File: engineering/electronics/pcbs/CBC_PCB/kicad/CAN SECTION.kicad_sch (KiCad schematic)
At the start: 44 parts, among them U25 ADM3053BRWZ-REEL7, U26 ADM3053BRWZ-REEL7, X1 8MHz, X2 8MHz

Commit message: fix: restore CBC schematic library nicknames
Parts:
- C10, C11, C3, C6: symbol CBC_PCB:CC0402JRNPO9BN220 -> EasyEDA_Lib:CC0402JRNPO9BN220
- C12, C48, C49, C5, C53, C54: symbol CBC_PCB:CL21A475KBQNNNE -> EasyEDA_Lib:CL21A475KBQNNNE
- C13, C4, C47, C50, C51, C55, C56, C57: symbol CBC_PCB:GRM21BR61H106KE43L -> EasyEDA_Lib:GRM21BR61H106KE43L
- C14, C2, C52, C58: symbol CBC_PCB:CC0402KRX7R7BB104 -> EasyEDA_Lib:CC0402KRX7R7BB104
- C16, C17, C8, C9: symbol CBC_PCB:GRM1555C1H221JA01D -> EasyEDA_Lib:GRM1555C1H221JA01D
- D1, D2: symbol CBC_PCB:NUP2105LT1G -> EasyEDA_Lib:NUP2105LT1G
- H1, H2: symbol CBC_PCB:PZ254V-11-02P -> EasyEDA_Lib:PZ254V-11-02P
- L1, L2: symbol CBC_PCB:ACT45B-510-2P-TF -> EasyEDA_Lib:ACT45B-510-2P-TF
- R1, R4: symbol CBC_PCB:0603WAF1200T5E -> EasyEDA_Lib:0603WAF1200T5E
- R2, R3: symbol CBC_PCB:RT0402BRD0710KL -> EasyEDA_Lib:RT0402BRD0710KL
- R34, R35: symbol CBC_PCB:RC0402FR-070RL -> EasyEDA_Lib:RC0402FR-070RL
- U25, U26: symbol CBC_PCB:ADM3053BRWZ-REEL7 -> EasyEDA_Lib:ADM3053BRWZ-REEL7
- U3, U5: symbol CBC_PCB:MCP2515T-I/ST -> EasyEDA_Lib:MCP2515T-I/ST
- X1, X2: symbol CBC_PCB:H1OEL89CSC-SUGYLC-8M -> EasyEDA_Lib:H1OEL89CSC-SUGYLC-8M
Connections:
- net +3V3: now also C12.2, C13.2, C14.2, C2.2, C4.2, C49.2, C5.2, C50.2, C53.2, C55.2, R2.2, R3.2, U25.6 (VIO), U26.6 (VIO), U3.20 (VDD), U5.20 (VDD)
- net +5V: now also C47.2, C48.2, C54.2, C56.2, U25.8 (VCC), U26.8 (VCC)
- net CANH_BAT: now also C8.2, D1.1, L1.2, R1.2
- net CANH_DRONE: now also C16.2, D2.1, L2.2, R4.2
- net CANL_BAT: now also C9.1, D1.2, H1.2, L1.3
- net CANL_DRONE: now also C17.1, D2.2, H2.2, L2.3
- net CS#1: now also U3.18 (CS#)
- net CS#2: now also U5.18 (CS#)
- net GND: now also C10.1, C11.1, C12.1, C13.1, C14.1, C2.1, C3.1, C4.1, C47.1, C48.1, C49.1, C5.1, C50.1, C53.1, C54.1, C55.1, C56.1, C6.1, U25.1 (GND1), U25.10 (GND1), U25.3 (GND1), U25.7 (GND1), U25.9 (GND1), U26.1 (GND1), U26.10 (GND1), U26.3 (GND1), U26.7 (GND1), U26.9 (GND1), U3.10 (VSS), U5.10 (VSS)
- net GND_CA: now also C51.1, C52.1, C8.1, C9.2, D1.3, R34.2, U25.11 (GND2), U25.13 (GND2), U25.16 (GND2), U25.20 (GND2)
- net GND_CB: now also C16.1, C17.2, C57.1, C58.1, D2.3, R35.2, U26.11 (GND2), U26.13 (GND2), U26.16 (GND2), U26.20 (GND2)
- net INT#1: now also U3.13 (INT#)
- net INT#2: now also U5.13 (INT#)
- net MISO: now also U3.17 (SO), U5.17 (SO)
- net MOSI: now also U3.16 (SI), U5.16 (SI)
- net RESET1: now also R2.1, U3.19 (RESET#)
- net RESET2: now also R3.1, U5.19 (RESET#)
- net RXD: now also U25.4 (RXD), U3.2 (RXCAN)
- net RXD2: now also U26.4 (RXD), U5.2 (RXCAN)
- net SCK: now also U3.14 (SCK), U5.14 (SCK)
- net TXD: now also U25.5 (TXD), U3.1 (TXCAN)
- net TXD2: now also U26.5 (TXD), U5.1 (TXCAN)
- new net: C51.2, C52.2, U25.12 (VISOOUT), U25.19 (VISOIN)
- new net: L1.4, U25.15 (CANL)
- new net: L1.1, U25.17 (CANH)
- new net: R34.1, U25.18 (RS)
- new net: C10.2, U5.9 (OSC1), X2.1 (OSC1)
- new net: C11.2, U5.8 (OSC2), X2.2 (OSC2)
- new net: H1.1, R1.1
- new net: C3.2, U3.9 (OSC1), X1.1 (OSC1)
- new net: C6.2, U3.8 (OSC2), X1.2 (OSC2)
- new net: R35.1, U26.18 (RS)
- new net: C57.2, C58.2, U26.12 (VISOOUT), U26.19 (VISOIN)
- new net: H2.1, R4.1
- new net: L2.4, U26.15 (CANL)
- new net: L2.1, U26.17 (CANH)
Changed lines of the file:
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@@
 	)
 	(symbol
-		(lib_id "CBC_PCB:GRM1555C1H221JA01D")
+		(lib_id "EasyEDA_Lib:GRM1555C1H221JA01D")
 		(at 323.85 196.85 90)
 		(unit 1)
@@
 	)
 	(symbol
-		(lib_id "CBC_PCB:ADM3053BRWZ-REEL7")
+		(lib_id "EasyEDA_Lib:ADM3053BRWZ-REEL7")
 		(at 220.98 55.88 0)
 		(unit 1)
@@
 	)
 	(symbol
-		(lib_id "CBC_PCB:CL21A475KBQNNNE")
+		(lib_id "EasyEDA_Lib:CL21A475KBQNNNE")
 		(at 196.85 201.93 90)
 		(unit 1)
@@
 	)
 	(symbol
-		(lib_id "CBC_PCB:GRM1555C1H221JA01D")
+		(lib_id "EasyEDA_Lib:GRM1555C1H221JA01D")
 		(at 314.96 59.69 90)
 		(unit 1)
@@
 	)
 	(symbol
-		(lib_id "CBC_PCB:H1OEL89CSC-SUGYLC-8M")
+		(lib_id "EasyEDA_Lib:H1OEL89CSC-SUGYLC-8M")
 		(at 41.91 215.9 0)
 		(unit 1)
@@
 	)
 	(symbol
-		(lib_id "CBC_PCB:0603WAF1200T5E")
+		(lib_id "EasyEDA_Lib:0603WAF1200T5E")
 		(at 302.26 49.53 90)
 		(unit 1)
@@
 	)
 	(symbol
-		(lib_id "CBC_PCB:RC0402FR-070RL")
+		(lib_id "EasyEDA_Lib:RC0402FR-070RL")
 		(at 248.92 36.83 0)
 		(unit 1)
@@
 	)
 	(symbol
-		(lib_id "CBC_PCB:GRM21BR61H106KE43L")
+		(lib_id "EasyEDA_Lib:GRM21BR61H106KE43L")
 		(at 207.01 203.2 90)
 		(unit 1)
@@
 	)
 	(symbol
-		(lib_id "CBC_PCB:H1OEL89CSC-SUGYLC-8M")
+		(lib_id "EasyEDA_Lib:H1OEL89CSC-SUGYLC-8M")
 		(at 44.45 74.93 0)
 		(unit 1)
@@
 	)
 	(symbol
-		(lib_id "CBC_PCB:RC0402FR-070RL")
+		(lib_id "EasyEDA_Lib:RC0402FR-070RL")
 		(at 265.43 172.72 0)
 		(unit 1)
@@
 	)
 	(symbol
-		(lib_id "CBC_PCB:NUP2105LT1G")
+		(lib_id "EasyEDA_Lib:NUP2105LT1G")
 		(at 335.28 214.63 180)
 		(unit 1)
@@
 	)
 	(symbol
-		(lib_id "CBC_PCB:CL21A475KBQNNNE")
+		(lib_id "EasyEDA_Lib:CL21A475KBQNNNE")
 		(at 175.26 49.53 90)
 		(unit 1)
@@
 	)
 	(symbol
-		(lib_id "CBC_PCB:ACT45B-510-2P-TF")
+		(lib_id "EasyEDA_Lib:ACT45B-510-2P-TF")
 		(at 289.56 54.61 0)
 		(unit 1)
@@
 	)
 	(symbol
-		(lib_id "CBC_PCB:CL21A475KBQNNNE")
+		(lib_id "EasyEDA_Lib:CL21A475KBQNNNE")
 		(at 180.34 66.04 90)
 		(unit 1)
@@
 	)
 	(symbol
-		(lib_id "CBC_PCB:CL21A475KBQNNNE")
+		(lib_id "EasyEDA_Lib:CL21A475KBQNNNE")
 		(at 191.77 185.42 90)
 		(unit 1)
@@
 	)
 	(symbol
-		(lib_id "CBC_PCB:GRM21BR61H106KE43L")
+		(lib_id "EasyEDA_Lib:GRM21BR61H106KE43L")
 		(at 278.13 207.01 90)
 		(unit 1)
@@
 	)
 	(symbol
-		(lib_id "CBC_PCB:NUP2105LT1G")
+		(lib_id "EasyEDA_Lib:NUP2105LT1G")
 		(at 326.39 77.47 180)
 		(unit 1)
@@
 	)
 	(symbol
-		(lib_id "CBC_PCB:0603WAF1200T5E")
+		(lib_id "EasyEDA_Lib:0603WAF1200T5E")
 		(at 311.15 186.69 90)
 		(unit 1)
@@
 	)
 	(symbol
-		(lib_id "CBC_PCB:PZ254V-11-02P")
+		(lib_id "EasyEDA_Lib:PZ254V-11-02P")
 		(at 316.23 194.31 0)
 		(unit 1)
@@
 	)
 	(symbol
-		(lib_id "CBC_PCB:PZ254V-11-02P")
+		(lib_id "EasyEDA_Lib:PZ254V-11-02P")
 		(at 307.34 57.15 0)
 		(unit 1)
@@
 	)
 	(symbol
-		(lib_id "CBC_PCB:GRM21BR61H106KE43L")
+		(lib_id "EasyEDA_Lib:GRM21BR61H106KE43L")
 		(at 185.42 50.8 90)
 		(unit 1)
@@
 	)
 	(symbol
-		(lib_id "CBC_PCB:GRM1555C1H221JA01D")
+		(lib_id "EasyEDA_Lib:GRM1555C1H221JA01D")
 		(at 323.85 185.42 90)
 		(unit 1)
@@
 	)
 	(symbol
-		(lib_id "CBC_PCB:GRM21BR61H106KE43L")
+		(lib_id "EasyEDA_Lib:GRM21BR61H106KE43L")
 		(at 190.5 67.31 90)
 		(unit 1)
@@
 	)
 	(symbol
-		(lib_id "CBC_PCB:GRM21BR61H106KE43L")
+		(lib_id "EasyEDA_Lib:GRM21BR61H106KE43L")
 		(at 100.33 92.71 90)
 		(unit 1)
@@
 	)
 	(symbol
-		(lib_id "CBC_PCB:CC0402KRX7R7BB104")
+		(lib_id "EasyEDA_Lib:CC0402KRX7R7BB104")
 		(at 107.95 92.71 90)
 		(unit 1)
@@
 	)
 	(symbol
-		(lib_id "CBC_PCB:CC0402JRNPO9BN220")
+		(lib_id "EasyEDA_Lib:CC0402JRNPO9BN220")
 		(at 54.61 219.71 90)
 		(unit 1)
@@
 	)
 	(symbol
-		(lib_id "CBC_PCB:CC0402JRNPO9BN220")
+		(lib_id "EasyEDA_Lib:CC0402JRNPO9BN220")
 		(at 57.15 78.74 90)
 		(unit 1)
@@
 	)
 	(symbol
-		(lib_id "CBC_PCB:CL21A475KBQNNNE")
+		(lib_id "EasyEDA_Lib:CL21A475KBQNNNE")
 		(at 87.63 232.41 90)
 		(unit 1)
@@
 	)
 	(symbol
-		(lib_id "CBC_PCB:CL21A475KBQNNNE")
+		(lib_id "EasyEDA_Lib:CL21A475KBQNNNE")
 		(at 90.17 91.44 90)
 		(unit 1)
@@
 	)
 	(symbol
-		(lib_id "CBC_PCB:GRM1555C1H221JA01D")
+		(lib_id "EasyEDA_Lib:GRM1555C1H221JA01D")
 		(at 314.96 48.26 90)
 		(unit 1)
@@
 	)
 	(symbol
-		(lib_id "CBC_PCB:MCP2515T-I/ST")
+		(lib_id "EasyEDA_Lib:MCP2515T-I/ST")
 		(at 100.33 54.61 0)
 		(unit 1)
@@
 	)
 	(symbol
-		(lib_id "CBC_PCB:MCP2515T-I/ST")
+		(lib_id "EasyEDA_Lib:MCP2515T-I/ST")
 		(at 97.79 195.58 0)
 		(unit 1)
@@
 	)
 	(symbol
-		(lib_id "CBC_PCB:GRM21BR61H106KE43L")
+		(lib_id "EasyEDA_Lib:GRM21BR61H106KE43L")
 		(at 261.62 71.12 90)
 		(unit 1)
@@
 	)
 	(symbol
-		(lib_id "CBC_PCB:RT0402BRD0710KL")
+		(lib_id "EasyEDA_Lib:RT0402BRD0710KL")
 		(at 69.85 27.94 90)
 		(unit 1)
@@
 	)
 	(symbol
-		(lib_id "CBC_PCB:CC0402KRX7R7BB104")
+		(lib_id "EasyEDA_Lib:CC0402KRX7R7BB104")
 		(at 105.41 233.68 90)
 		(unit 1)
@@
 	)
 	(symbol
-		(lib_id "CBC_PCB:CC0402KRX7R7BB104")
+		(lib_id "EasyEDA_Lib:CC0402KRX7R7BB104")
 		(at 284.48 207.01 90)
 		(unit 1)
@@
 	)
 	(symbol
-		(lib_id "CBC_PCB:RT0402BRD0710KL")
+		(lib_id "EasyEDA_Lib:RT0402BRD0710KL")
 		(at 67.31 168.91 90)
 		(unit 1)
@@
 	)
 	(symbol
-		(lib_id "CBC_PCB:CC0402JRNPO9BN220")
+		(lib_id "EasyEDA_Lib:CC0402JRNPO9BN220")
 		(at 30.48 78.74 90)
 		(unit 1)
@@
 	)
 	(symbol
-		(lib_id "CBC_PCB:GRM21BR61H106KE43L")
+		(lib_id "EasyEDA_Lib:GRM21BR61H106KE43L")
 		(at 201.93 186.69 90)
 		(unit 1)
@@
 	)
 	(symbol
-		(lib_id "CBC_PCB:GRM21BR61H106KE43L")
+		(lib_id "EasyEDA_Lib:GRM21BR61H106KE43L")
 		(at 97.79 233.68 90)
 		(unit 1)
@@
 	)
 	(symbol
-		(lib_id "CBC_PCB:ADM3053BRWZ-REEL7")
+		(lib_id "EasyEDA_Lib:ADM3053BRWZ-REEL7")
 		(at 237.49 191.77 0)
 		(unit 1)
@@
 	)
 	(symbol
-		(lib_id "CBC_PCB:CC0402KRX7R7BB104")
+		(lib_id "EasyEDA_Lib:CC0402KRX7R7BB104")
 		(at 267.97 71.12 90)
 		(unit 1)
@@
 	)
 	(symbol
-		(lib_id "CBC_PCB:CC0402JRNPO9BN220")
+		(lib_id "EasyEDA_Lib:CC0402JRNPO9BN220")
 		(at 27.94 219.71 90)
 		(unit 1)
@@
 	)
 	(symbol
-		(lib_id "CBC_PCB:ACT45B-510-2P-TF")
+		(lib_id "EasyEDA_Lib:ACT45B-510-2P-TF")
 		(at 298.45 191.77 0)
 		(unit 1)

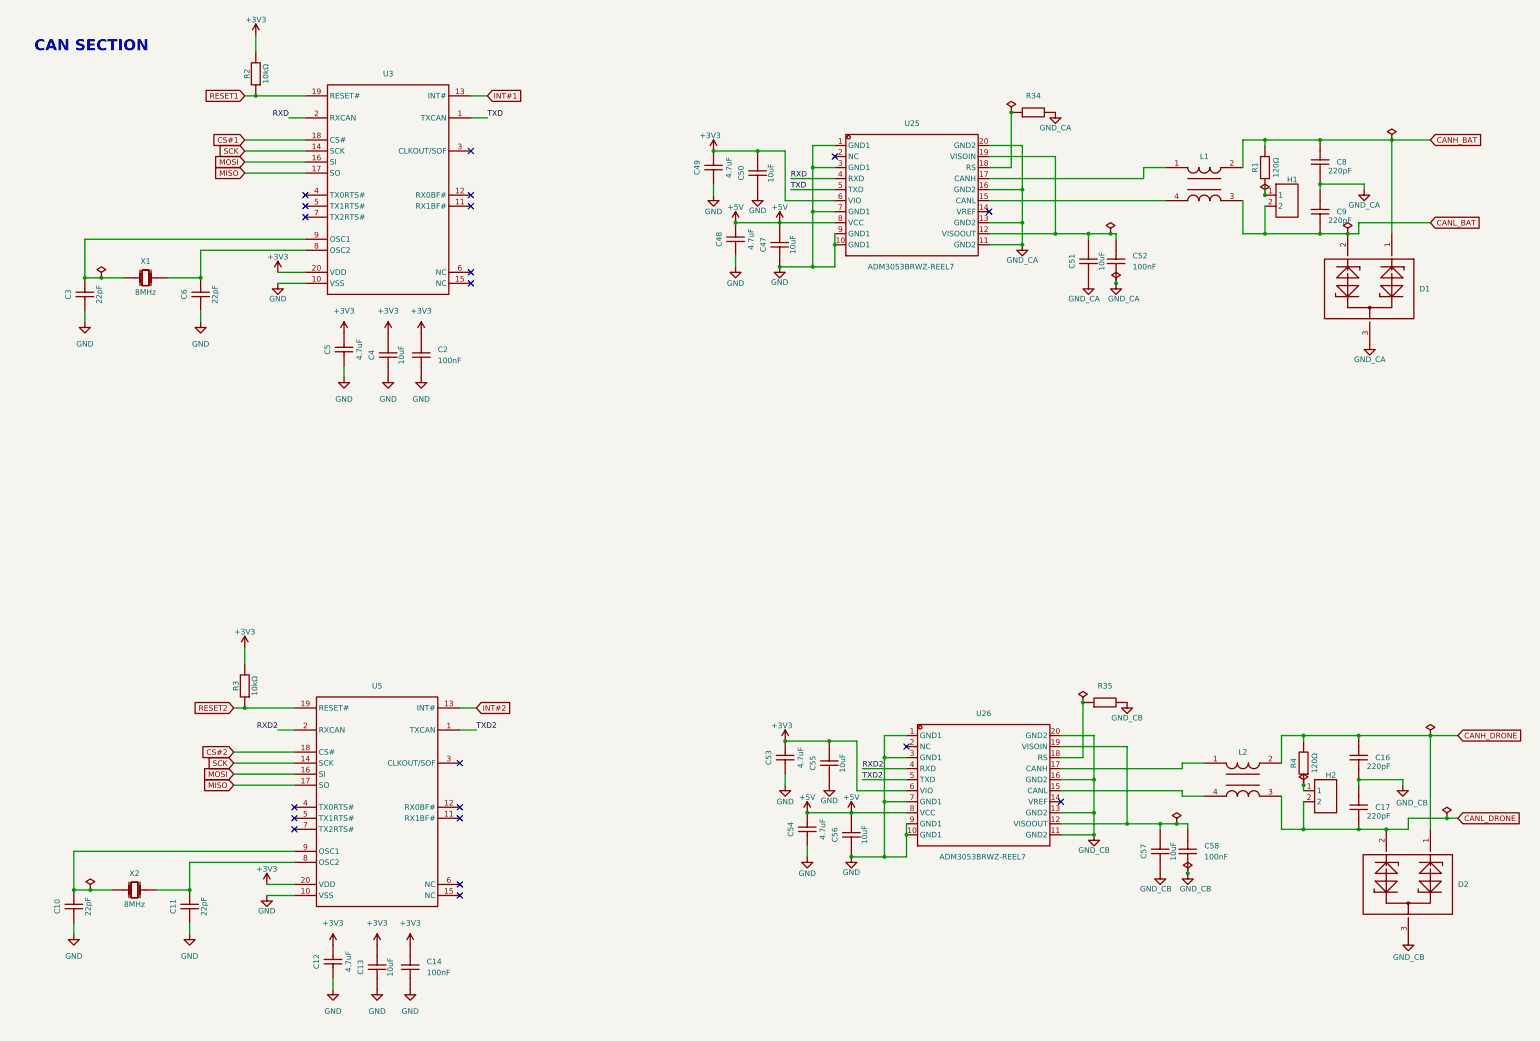
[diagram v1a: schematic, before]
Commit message: fix: assign CBC imported symbol pin types
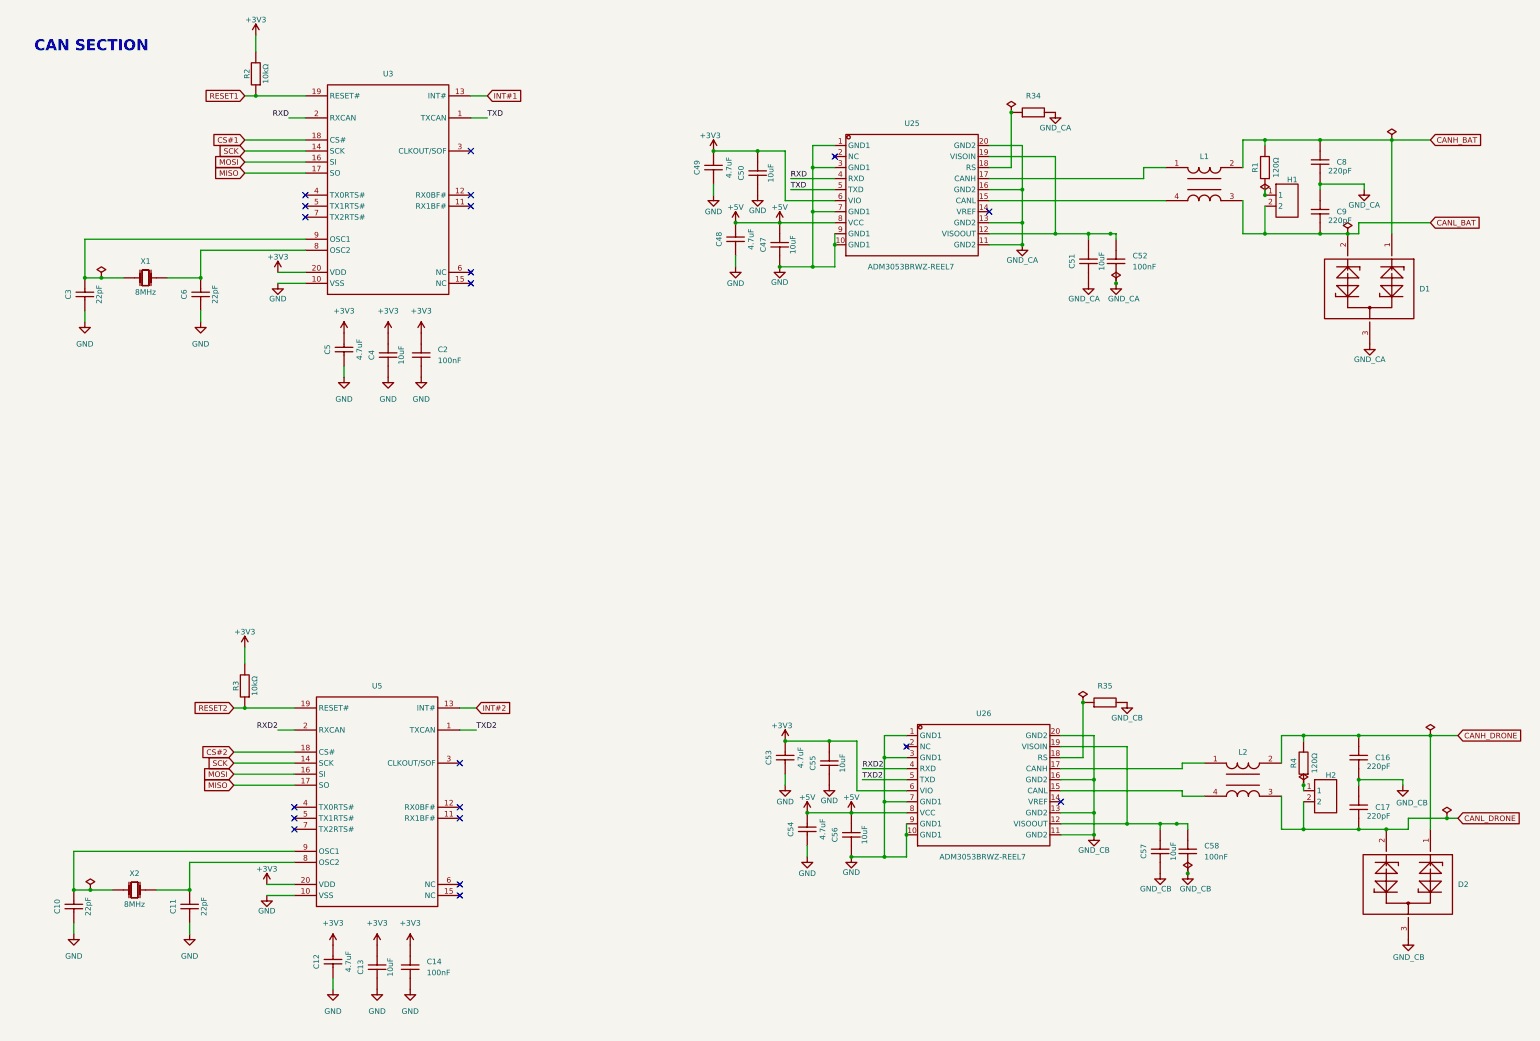
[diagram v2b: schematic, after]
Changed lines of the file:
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@@
-	)
-	(symbol
-		(lib_id "power:PWR_FLAG")
-		(at 266.7 64.77 0)
-		(unit 1)
-		(body_style 1)
-		(exclude_from_sim no)
-		(in_bom yes)
-		(on_board yes)
-		(in_pos_files yes)
-		(dnp no)
-		(fields_autoplaced yes)
-		(property "Reference" "#FLG063"
-			(at 266.7 62.865 0)
-			(hide yes)
-			(show_name no)
-			(do_not_autoplace no)
-			(effects
-				(font
-					(size 1.27 1.27)
-				)
-			)
-		)
-		(property "Value" "PWR_FLAG"
-			(at 266.7 59.69 0)
-			(hide yes)
-			(show_name no)
-			(do_not_autoplace no)
-			(effects
-				(font
-					(size 1.27 1.27)
-				)
-			)
-		)
-		(property "Footprint" ""
-			(at 266.7 64.77 0)
-			(hide yes)
-			(show_name no)
-			(do_not_autoplace no)
-			(effects
-				(font
-					(size 1.27 1.27)
-				)
-			)
-		)
-		(property "Datasheet" ""
-			(at 266.7 64.77 0)
-			(hide yes)
-			(show_name no)
-			(do_not_autoplace no)
-			(effects
-				(font
-					(size 1.27 1.27)
-				)
-			)
-		)
-		(property "Description" "Special symbol for telling ERC where power comes from"
-			(at 266.7 64.77 0)
-			(hide yes)
-			(show_name no)
-			(do_not_autoplace no)
-			(effects
-				(font
-					(size 1.27 1.27)
-				)
-			)
-		)
-		(pin "1"
-		)
-		(instances
-			(project "CBC_PCB"
-				(path "/d195d1ee-585b-4211-912f-f5dd5687bc63/313c40c6-0a26-497a-98c9-c78a7bba0e9e"
-					(reference "#FLG063")
-					(unit 1)
-				)
-			)
-		)
 	)
 	(symbol
@@
 					(unit 1)
 				)
-			)
-		)
-	)
-	(symbol
-		(lib_id "power:PWR_FLAG")
-		(at 281.94 200.66 0)
-		(unit 1)
-		(body_style 1)
-		(exclude_from_sim no)
-		(in_bom yes)
-		(on_board yes)
-		(in_pos_files yes)
-		(dnp no)
-		(fields_autoplaced yes)
-		(property "Reference" "#FLG055"
-			(at 281.94 198.755 0)
-			(hide yes)
-			(show_name no)
-			(do_not_autoplace no)
-			(effects
-				(font
-					(size 1.27 1.27)
-				)
-			)
-		)
-		(property "Value" "PWR_FLAG"
-			(at 281.94 195.58 0)
-			(hide yes)
-			(show_name no)
-			(do_not_autoplace no)
-			(effects
-				(font
-					(size 1.27 1.27)
-				)
-			)
-		)
-		(property "Footprint" ""
-			(at 281.94 200.66 0)
-			(hide yes)
-			(show_name no)
-			(do_not_autoplace no)
-			(effects
-				(font
-					(size 1.27 1.27)
-				)
-			)
-		)
-		(property "Datasheet" ""
-			(at 281.94 200.66 0)
-			(hide yes)
-			(show_name no)
-			(do_not_autoplace no)
-			(effects
-				(font
-					(size 1.27 1.27)
-				)
-			)
-		)
-		(property "Description" "Special symbol for telling ERC where power comes from"
-			(at 281.94 200.66 0)
-			(hide yes)
-			(show_name no)
-			(do_not_autoplace no)
-			(effects
-				(font
-					(size 1.27 1.27)
-				)
-			)
-		)
-		(pin "1"
-		)
-		(instances
-			(project "CBC_PCB"
-				(path "/d195d1ee-585b-4211-912f-f5dd5687bc63/313c40c6-0a26-497a-98c9-c78a7bba0e9e"
-					(reference "#FLG055")
-					(unit 1)
-				)

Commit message: docs: capture CBC schematic review follow-ups
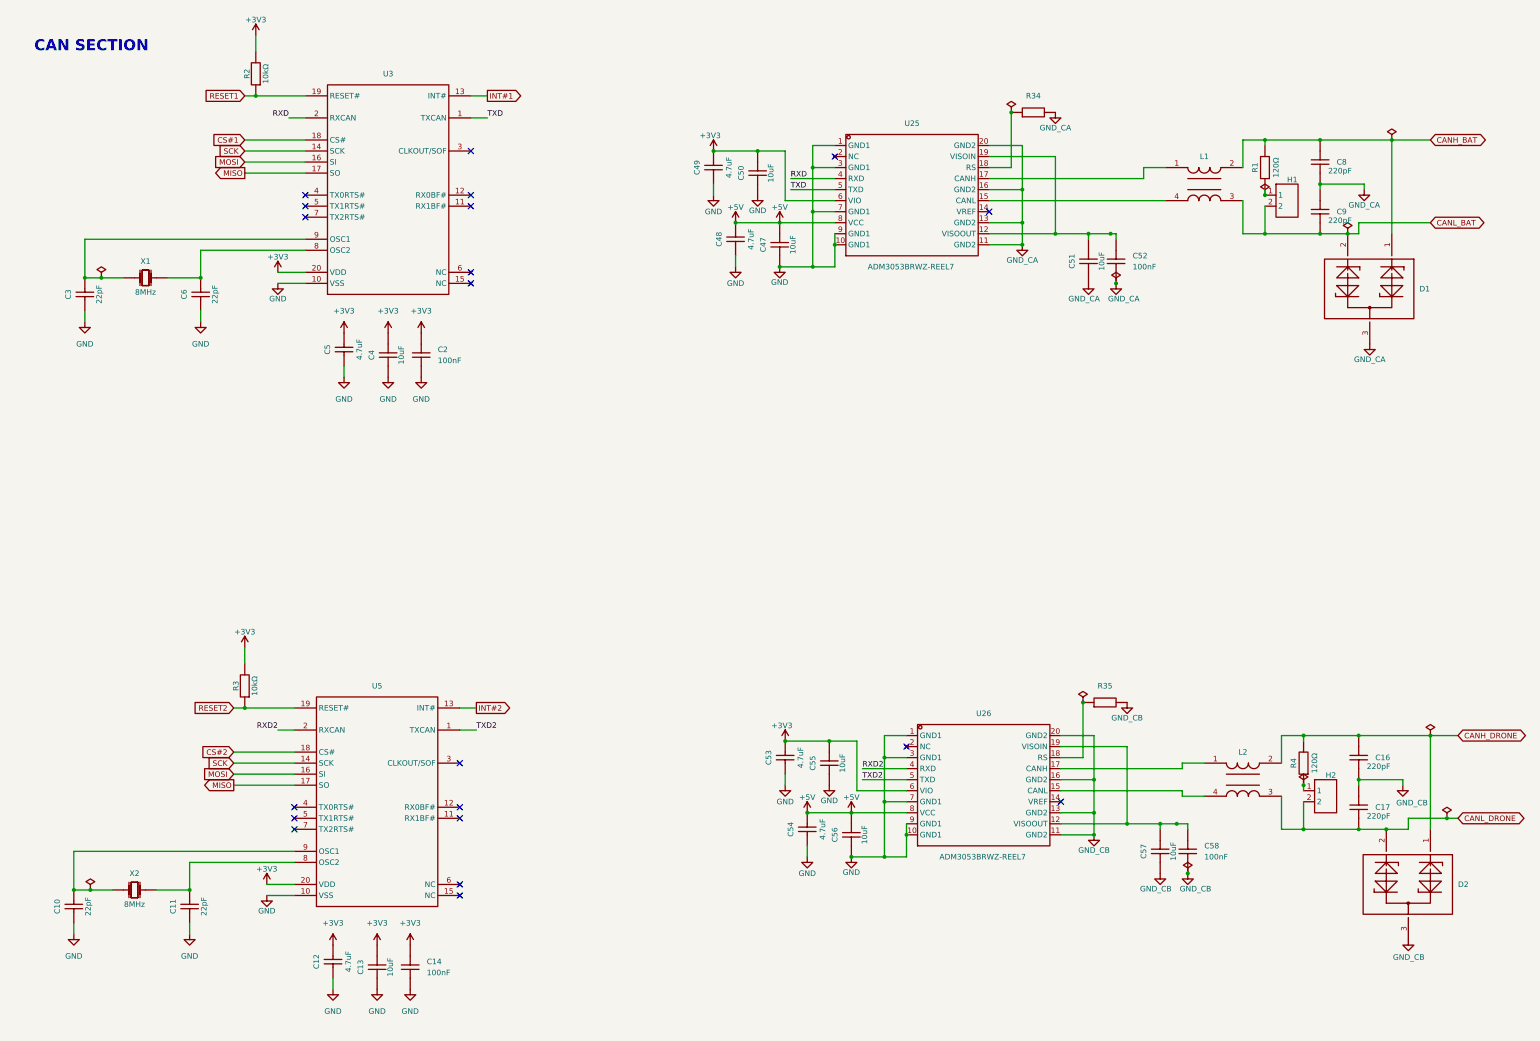
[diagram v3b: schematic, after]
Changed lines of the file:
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@@
 	)
 	(global_label "INT#2"
-		(shape input)
+		(shape output)
 		(at 120.65 173.99 0)
 		(fields_autoplaced yes)
@@
 	)
 	(global_label "CANL_BAT"
-		(shape input)
+		(shape bidirectional)
 		(at 340.36 62.23 0)
 		(fields_autoplaced yes)
@@
 	)
 	(global_label "MISO"
-		(shape input)
+		(shape output)
 		(at 64.77 191.77 180)
 		(fields_autoplaced yes)
@@
 	)
 	(global_label "CANH_DRONE"
-		(shape input)
+		(shape bidirectional)
 		(at 346.71 180.34 0)
 		(fields_autoplaced yes)
@@
 	)
 	(global_label "MISO"
-		(shape input)
+		(shape output)
 		(at 67.31 50.8 180)
 		(fields_autoplaced yes)
@@
 	)
 	(global_label "CANH_BAT"
-		(shape input)
+		(shape bidirectional)
 		(at 340.36 43.18 0)
 		(fields_autoplaced yes)
@@
 	)
 	(global_label "INT#1"
-		(shape input)
+		(shape output)
 		(at 123.19 33.02 0)
 		(fields_autoplaced yes)
@@
 	)
 	(global_label "CANL_DRONE"
-		(shape input)
+		(shape bidirectional)
 		(at 346.71 199.39 0)
 		(fields_autoplaced yes)
